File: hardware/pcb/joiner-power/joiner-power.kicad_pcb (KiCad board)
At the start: 2 copper layers, 105.2 x 82.6 mm, 9 parts, among them J1 Mains in, J2 Main out, J3 Control, K1 SLA-05VDC-SL-A

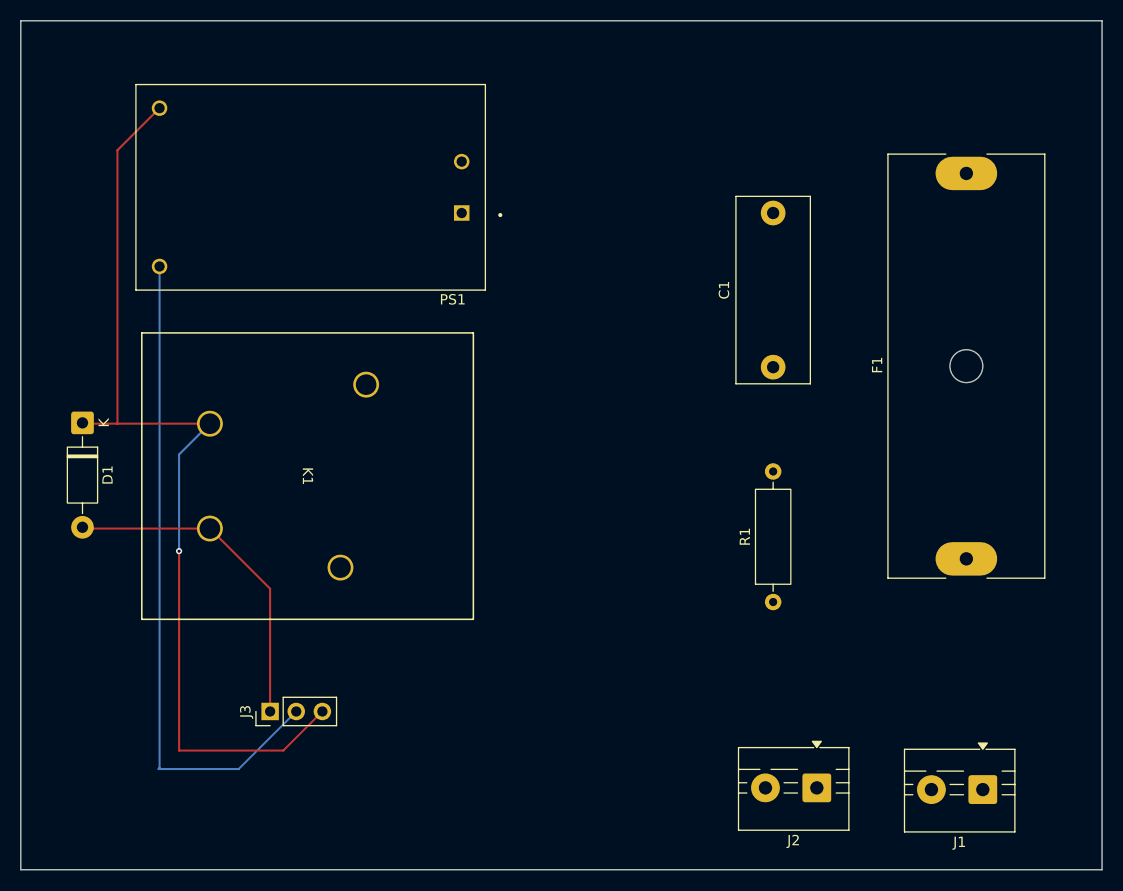
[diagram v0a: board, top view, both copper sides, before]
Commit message: Began PCB BOM
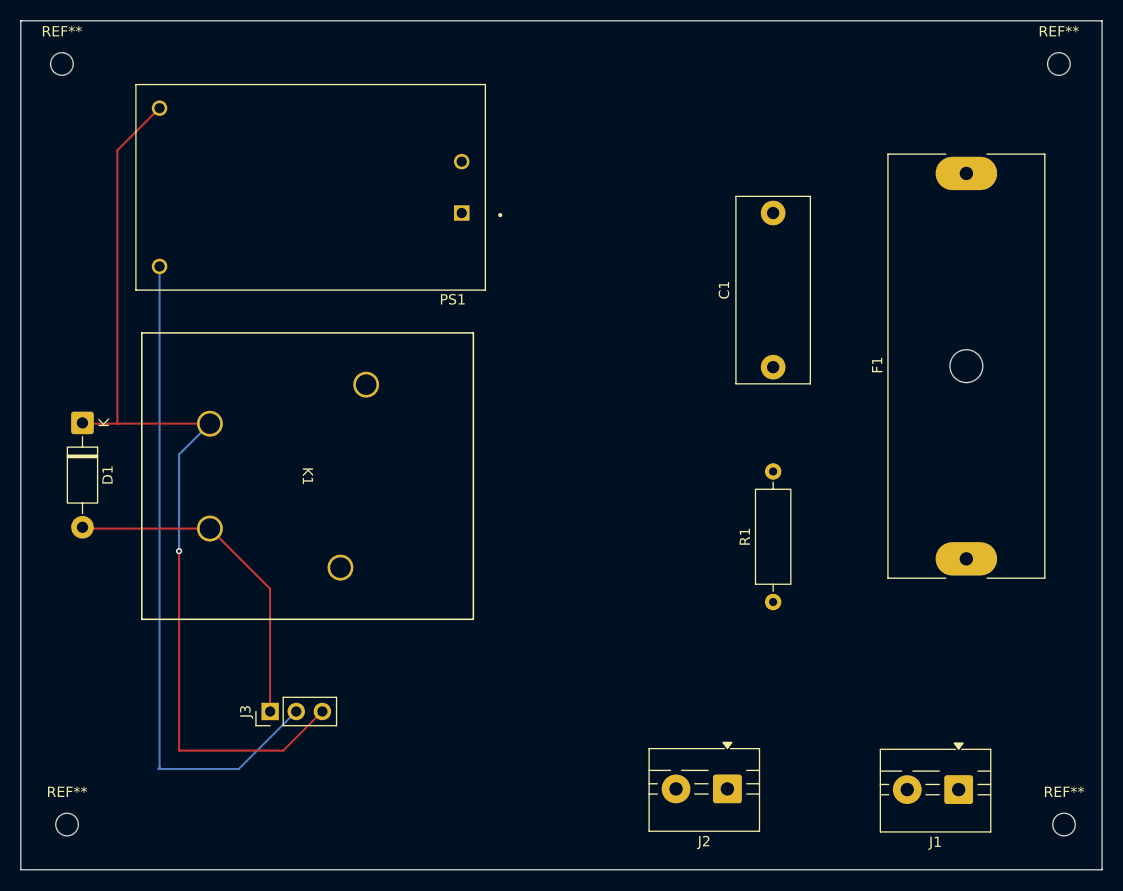
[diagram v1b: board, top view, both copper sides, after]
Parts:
- added REF**: M2, MountingHole:MountingHole_2.2mm_M2, F.Cu at (104.5, 122.0)
- added REF**: M2, MountingHole:MountingHole_2.2mm_M2, F.Cu at (104.0, 48.0)
- added REF**: M2, MountingHole:MountingHole_2.2mm_M2, F.Cu at (201.5, 122.0)
- added REF**: M2, MountingHole:MountingHole_2.2mm_M2, F.Cu at (201.0, 48.0)
- moved J2 8.70 mm to (168.8, 118.5)
- moved J1 2.35 mm to (191.2, 118.6)
